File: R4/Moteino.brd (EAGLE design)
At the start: 33.3 x 23.1 mm, 22 parts, among them IC3 MCP1703CB, X1 16 MHz

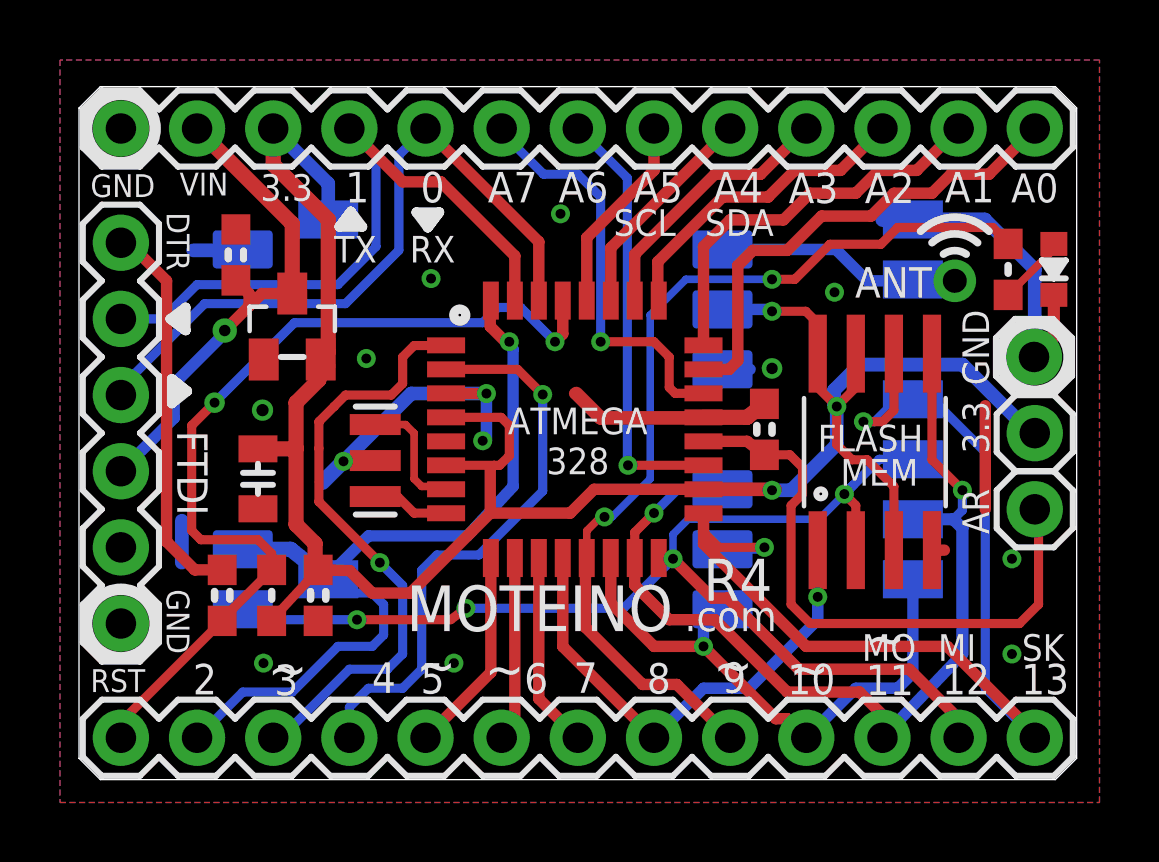
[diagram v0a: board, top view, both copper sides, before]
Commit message: Connect pin 3 with DIO2 https://github.com/kobuki/RFM69OOK
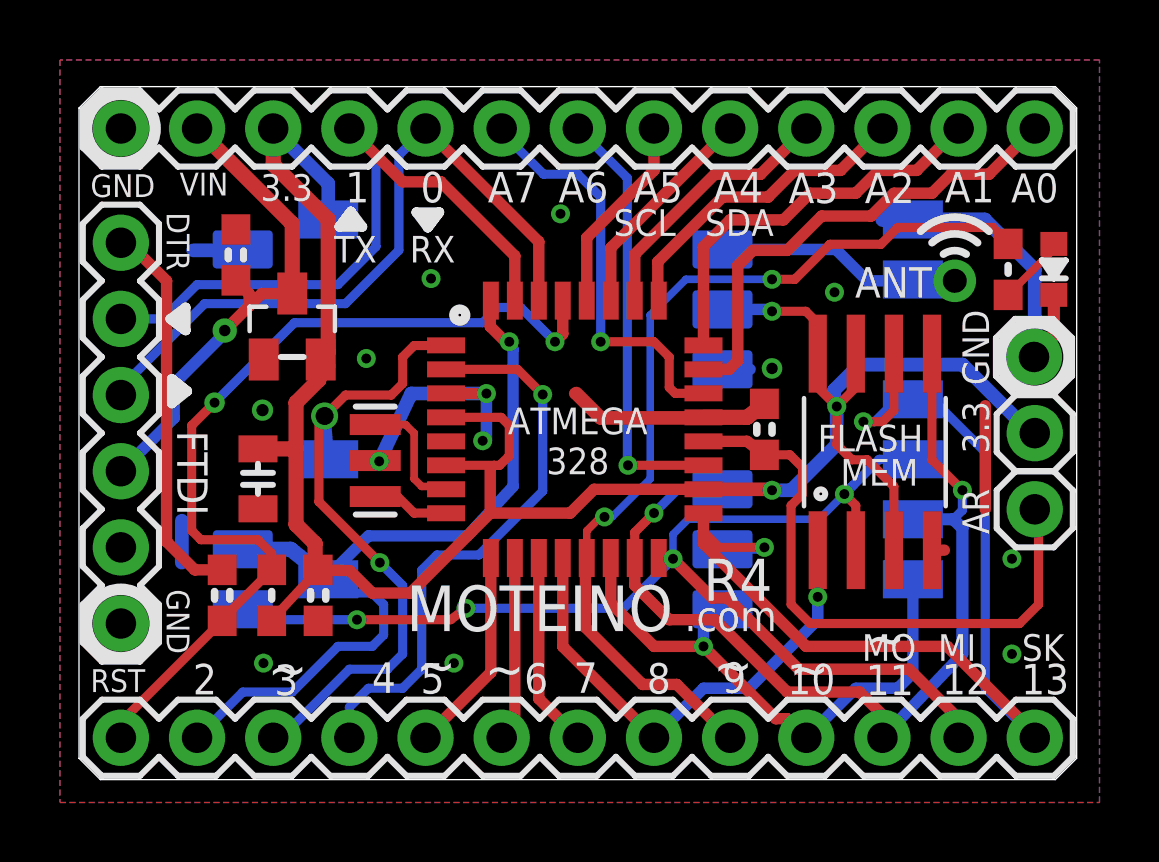
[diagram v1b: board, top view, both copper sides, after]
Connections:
- net D3: now also U$5.DIO2
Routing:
- net GND: track 37.9 -> 35.2 mm
- net D3: track 20.2 -> 21.6 mm, vias 1 -> 2
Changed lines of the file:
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@@
 <?xml version="1.0" encoding="utf-8"?>
 <!DOCTYPE eagle SYSTEM "eagle.dtd">
-<eagle version="6.5.0">
+<eagle version="7.4.0">
 <drawing>
 <settings>
@@
 <layer number="54" name="bGND_GNDA" color="1" fill="9" visible="no" active="no"/>
 <layer number="56" name="wert" color="7" fill="1" visible="no" active="yes"/>
+<layer number="90" name="Modules" color="5" fill="1" visible="no" active="no"/>
 <layer number="91" name="Nets" color="2" fill="1" visible="no" active="no"/>
 <layer number="92" name="Busses" color="1" fill="1" visible="no" active="no"/>
@@
 <pass name="Default">
 <param name="RoutingGrid" value="50mil"/>
+<param name="AutoGrid" value="1"/>
+<param name="Efforts" value="0"/>
+<param name="TopRouterVariant" value="1"/>
 <param name="tpViaShape" value="round"/>
 <param name="PrefDir.1" value="|"/>
@@
 <contactref element="ATMEGA328" pad="5"/>
 <via x="6.1207" y="12.3242" extent="1-16" drill="0.4064"/>
-<via x="8.8203" y="10.6172" extent="1-16" drill="0.3302"/>
+<via x="10.0141" y="10.6172" extent="1-16" drill="0.3302"/>
 <contactref element="JP2" pad="1"/>
 <contactref element="C5" pad="2"/>
@@
 <wire x1="16.5292" y1="12.8778" x2="16.5862" y2="12.8778" width="0.381" layer="1"/>
 <wire x1="16.5862" y1="12.8778" x2="17.399" y2="12.065" width="0.4572" layer="1"/>
-<wire x1="31.877" y1="14.1224" x2="31.8516" y2="14.097" width="0.4572" layer="16"/>
 <via x="23.114" y="13.716" extent="1-16" drill="0.381"/>
 <wire x1="22.987" y1="12.407" x2="22.86" y2="12.534" width="0.508" layer="1"/>
@@
 <wire x1="31.877" y1="17.018" x2="31.877" y2="14.1224" width="0.4572" layer="16"/>
 <wire x1="31.877" y1="14.1224" x2="31.8516" y2="14.097" width="0.4572" layer="16"/>
-<wire x1="8.1143" y1="9.9112" x2="8.8203" y2="10.6172" width="0.508" layer="16"/>
-<wire x1="8.8203" y1="10.6172" x2="11.0809" y2="12.8778" width="0.4572" layer="16"/>
+<wire x1="10.0193" y1="10.597" x2="10.0141" y2="10.6172" width="0.508" layer="16"/>
+<wire x1="10.0141" y1="10.6172" x2="11.0809" y2="12.8778" width="0.4572" layer="16"/>
 <wire x1="11.0809" y1="12.8778" x2="13.589" y2="12.8778" width="0.4572" layer="16"/>
 <wire x1="3.429" y1="8.636" x2="3.429" y2="7.239" width="0.4572" layer="16"/>
@@
 <via x="11.7413" y="16.7132" extent="1-16" drill="0.3302"/>
 <via x="16.0593" y="18.8722" extent="1-16" drill="0.3302"/>
-<wire x1="8.8203" y1="10.6172" x2="9.8806" y2="10.6426" width="0.381" layer="1"/>
+<wire x1="10.0141" y1="10.6172" x2="9.8806" y2="10.6426" width="0.381" layer="1"/>
 <via x="25.1968" y="16.256" extent="1-16" drill="0.3302"/>
 <via x="31.115" y="7.366" extent="1-16" drill="0.3302"/>
@@
 <via x="10.033" y="7.239" extent="1-16" drill="0.3302"/>
 <wire x1="12.2368" y1="14.478" x2="12.2428" y2="14.484" width="0.381" layer="1"/>
-<wire x1="8.001" y1="11.938" x2="8.001" y2="11.049" width="0.3048" layer="1"/>
-<wire x1="8.001" y1="11.049" x2="8.001" y2="9.271" width="0.3048" layer="1"/>
+<wire x1="8.001" y1="11.938" x2="8.001" y2="9.271" width="0.3048" layer="1"/>
 <wire x1="8.001" y1="9.271" x2="10.033" y2="7.239" width="0.3048" layer="1"/>
 <wire x1="6.477" y1="1.397" x2="6.731" y2="1.397" width="0.3048" layer="16"/>
@@
 <wire x1="10.795" y1="4.191" x2="10.795" y2="6.477" width="0.3048" layer="16"/>
 <wire x1="10.795" y1="6.477" x2="10.033" y2="7.239" width="0.3048" layer="16"/>
-<wire x1="8.001" y1="11.938" x2="8.509" y2="12.446" width="0.3048" layer="1"/>
-<wire x1="8.509" y1="12.446" x2="8.89" y2="12.827" width="0.3048" layer="1"/>
+<wire x1="8.001" y1="11.938" x2="8.1915" y2="12.1285" width="0.3048" layer="1"/>
+<wire x1="8.2042" y1="12.1412" x2="8.89" y2="12.827" width="0.3048" layer="1"/>
 <wire x1="8.89" y1="12.827" x2="10.414" y2="12.827" width="0.3048" layer="1"/>
 <wire x1="10.414" y1="12.827" x2="10.795" y2="13.208" width="0.3048" layer="1"/>
@@
 <wire x1="10.795" y1="14.097" x2="11.176" y2="14.478" width="0.3048" layer="1"/>
 <wire x1="11.176" y1="14.478" x2="12.2368" y2="14.478" width="0.3048" layer="1"/>
-<wire x1="12.2368" y1="14.478" x2="12.2428" y2="14.484" width="0.3048" layer="1"/>
+<contactref element="U$5" pad="DIO2"/>
+<wire x1="8.312" y1="10.684" x2="8.1915" y2="12.1285" width="0.4064" layer="16"/>
+<via x="8.1915" y="12.1285" extent="1-16" drill="0.6"/>
+<wire x1="8.1915" y1="12.1285" x2="8.2042" y2="12.1412" width="0.4064" layer="1"/>
 </signal>
 <signal name="D1_TX">

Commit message: add capacitor values
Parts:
- C1, C4, C5: value 0.1 -> 0.1uF
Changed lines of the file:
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@@
 <element name="JP2" library="SparkFun-Connectors" package="1X01" value="M01PTH" x="31.8516" y="14.097" smashed="yes"/>
 <element name="+" library="SparkFun-Connectors" package="1X01" value="M01PTH" x="31.877" y="11.557" smashed="yes" rot="R270"/>
-<element name="C5" library="LowPowerLab" package="0603-CAP" value="0.1" x="22.86" y="11.684" smashed="yes" rot="R90">
+<element name="C5" library="LowPowerLab" package="0603-CAP" value="0.1uF" x="22.86" y="11.684" smashed="yes" rot="R90">
 <attribute name="VALUE" x="24.0157" y="14.1224" size="0.889" layer="51" font="vector" ratio="15" rot="R180"/>
 </element>
@@
 <attribute name="VALUE" x="7.7216" y="5.0927" size="0.762" layer="51" ratio="15" rot="R90"/>
 </element>
-<element name="C1" library="LowPowerLab" package="0603-CAP" value="0.1" x="4.7752" y="6.1468" smashed="yes" rot="R90">
+<element name="C1" library="LowPowerLab" package="0603-CAP" value="0.1uF" x="4.7752" y="6.1468" smashed="yes" rot="R90">
 <attribute name="VALUE" x="6.1468" y="5.1181" size="0.762" layer="51" ratio="15" rot="R90"/>
 </element>
-<element name="C4" library="LowPowerLab" package="0603-CAP" value="0.1" x="7.9756" y="6.1468" smashed="yes" rot="R270">
+<element name="C4" library="LowPowerLab" package="0603-CAP" value="0.1uF" x="7.9756" y="6.1468" smashed="yes" rot="R270">
 <attribute name="VALUE" x="7.62" y="9.3853" size="0.762" layer="51" ratio="15" rot="R270"/>
 </element>
